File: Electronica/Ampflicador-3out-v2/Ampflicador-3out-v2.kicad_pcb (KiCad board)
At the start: 2 copper layers, 42 parts, among them P1 Piezo 1, P2 Piezo 2, P3 Piezo 2, Q1 MPF102, SW1 SW_DPST_x2, SW2 SW_DPST_x2, SW3 SW_SPDT, U1 LM386

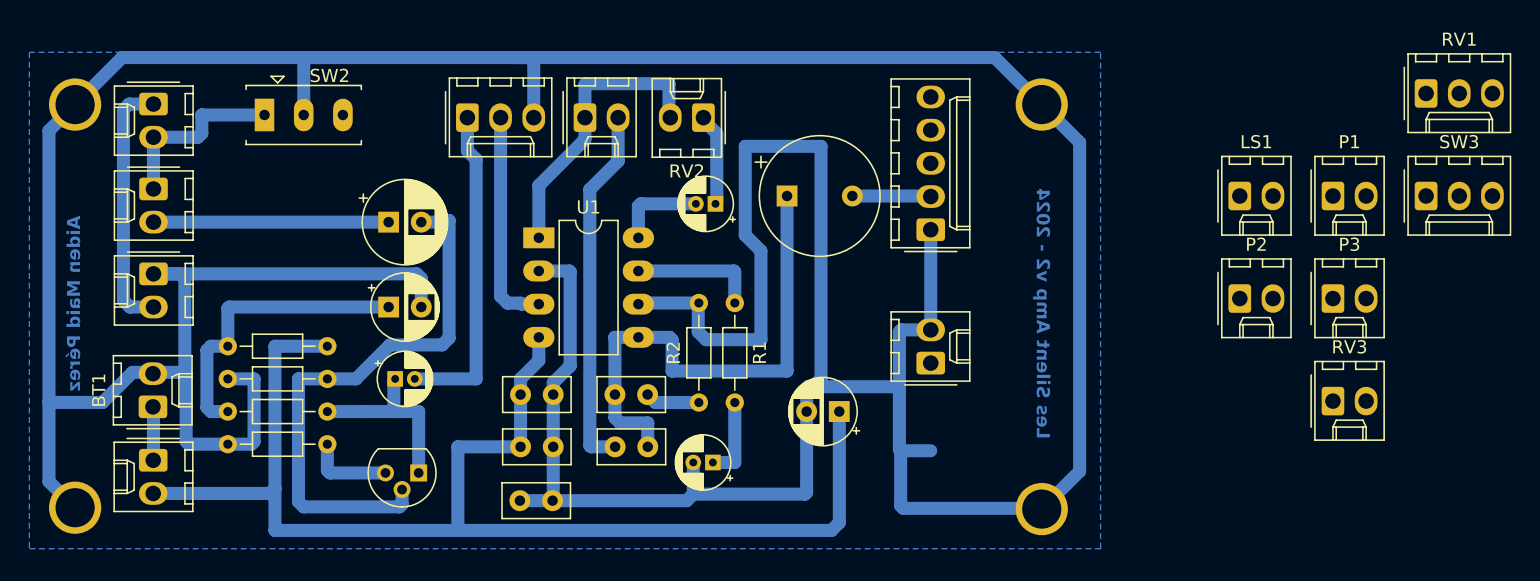
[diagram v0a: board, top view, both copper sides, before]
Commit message: Amp v2 sin termianr
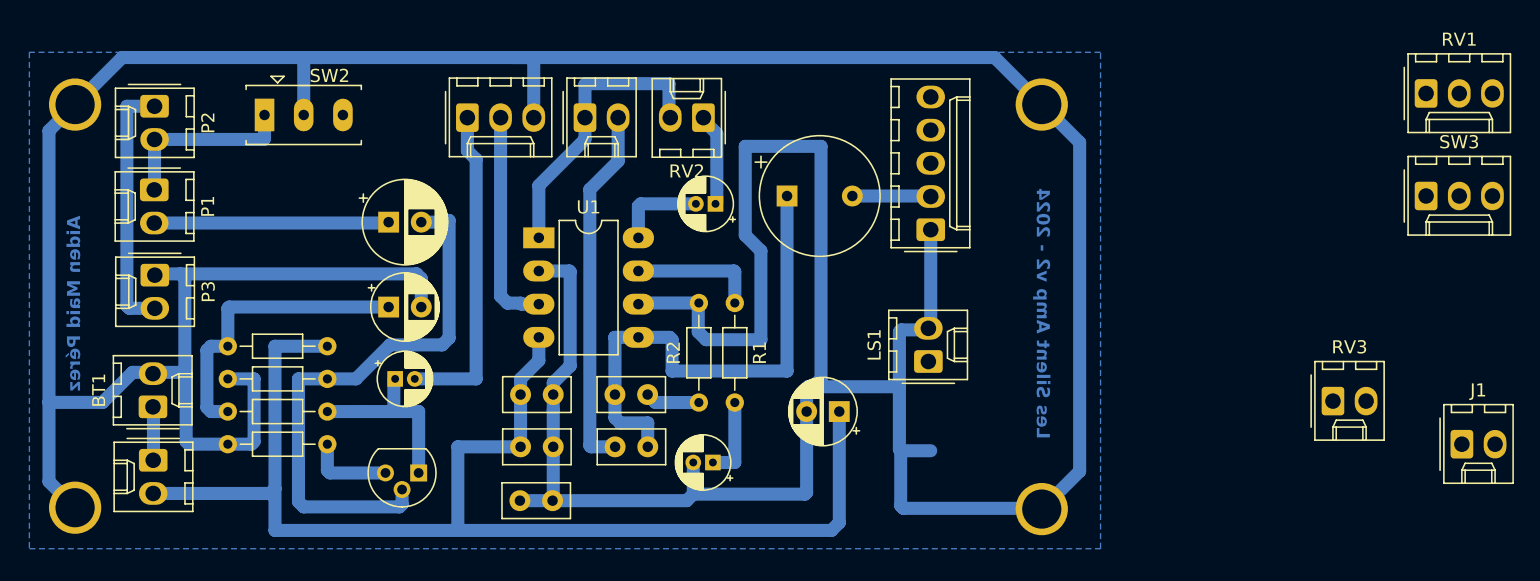
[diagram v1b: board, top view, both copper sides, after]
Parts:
- removed Input1, Input2, Input3, Output-Speaker1: Screw_Terminal_01x02, Connector_Molex:Molex_KK-254_AE-6410-02A_1x02_P2.54mm_Vertical
- added J1: Jack 6.5, Connector_Molex:Molex_KK-254_AE-6410-02A_1x02_P2.54mm_Vertical, F.Cu at (129.7, 54.0)
- moved P1 90.2 mm to (29.6, 34.5), turned to -90 degrees
- moved P3 90.2 mm to (29.6, 41.1), turned to -90 degrees
- moved P2 84.4 mm to (29.6, 28.1), turned to -90 degrees
- moved LS1 27.0 mm to (88.8, 47.7), turned to 90 degrees
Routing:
- net Net-(P2-Pad1): track 0.00 -> 19.6 mm
- net Net-(Input2-Pin_1): track 19.6 -> 0.00 mm
- net Net-(Input1-Pin_2): track 18.0 -> 0.00 mm
- net Net-(C10-Pad1): track 0.00 -> 18.0 mm
- net Net-(SW2A-A): track 0.00 -> 14.1 mm
- net Net-(Input1-Pin_1): track 14.0 -> 0.00 mm
- net GND: track 366.2 -> 364.2 mm

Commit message: Amp creo que para imprimir
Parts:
- removed Bass1: Screw_Terminal_01x02, Connector_Molex:Molex_KK-254_AE-6410-02A_1x02_P2.54mm_Vertical
- removed SW3: SW_SPDT, Connector_Molex:Molex_KK-254_AE-6410-03A_1x03_P2.54mm_Vertical
- removed Vol1: Screw_Terminal_01x03, Connector_Molex:Molex_KK-254_AE-6410-03A_1x03_P2.54mm_Vertical
- Gain: renamed from RV2; value Gain -> (none)
- J1: renamed from Output-Jack-3.5; value AudioJack2_Ground_Switch -> (none)
- J2: renamed from J1; value Jack 6.5 -> (none)
- LM386: renamed from U1; value LM386 -> (none)
- P2: value Piezo 2 -> (none)
- SP1: renamed from LS1; value Speaker -> (none)
- SW2: value SW_DPST_x2 -> (none)
- Volume: renamed from RV1; value Volume -> (none)
- moved Volume 73.5 mm to (53.5, 29.0)
- moved Bass 61.2 mm to (62.5, 29.0)
- moved J2 40.9 mm to (88.8, 54.5), turned to 90 degrees
- moved PW 2.61 mm to (29.5, 48.5), turned to -90 degrees
- moved Gain 2.50 mm to (69.1, 29.0), turned to 0 degrees
- moved C2 2.41 mm to (79.6, 51.4), turned to 0 degrees
- moved ? 1.70 mm to (95.8, 59.0)
- moved ? 1.70 mm to (95.8, 28.0)
- moved C6 0.22 mm to (72.3, 35.7)
- renumbered RV3 to Bass, BT1 to PW
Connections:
- J1 pad 2: (no net) -> Net-(C9-Pad2)
- J1 pad 3: (no net) -> Net-(J1-PadT)
- J1 pad 4: (no net) -> Net-(J1-PadT)
- J1 pad 5: (no net) -> Net-(C9-Pad2)
- J2 pad 1: (no net) -> GND
- J2 pad 2: (no net) -> Net-(J1-PadT)
- SP1 pad 1: Net-(SW3-C) -> Net-(J1-PadT)
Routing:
- net GND: track 364.2 -> 249.3 mm
- net Net-(J1-PadT): track 0.00 -> 30.3 mm
- net Net-(C8-Pad1): track 0.00 -> 28.0 mm
- net Net-(Bass1-Pin_2): track 28.0 -> 0.00 mm
- net Net-(RV2-Pad2): track 0.00 -> 25.2 mm
- net Net-(Vol1-Pin_1): track 24.9 -> 0.00 mm
- net Net-(C12-Pad2): track 0.00 -> 24.9 mm
- net Net-(Bass1-Pin_1): track 22.3 -> 0.00 mm
- net Net-(C9-Pad2): track 6.02 -> 16.7 mm
- net Net-(BT1-+): track 4.20 -> 12.0 mm
- net Net-(SW1A-B): track 99.5 -> 97.0 mm
- net Net-(C6-Pad1): track 7.12 -> 9.42 mm
- net Net-(SW2A-A): track 14.1 -> 16.0 mm
- net Net-(P2-Pad1): track 19.6 -> 21.4 mm
- net Net-(Q1-G): track 42.4 -> 43.4 mm
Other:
- board outline added: 79.8 x 38.4 mm

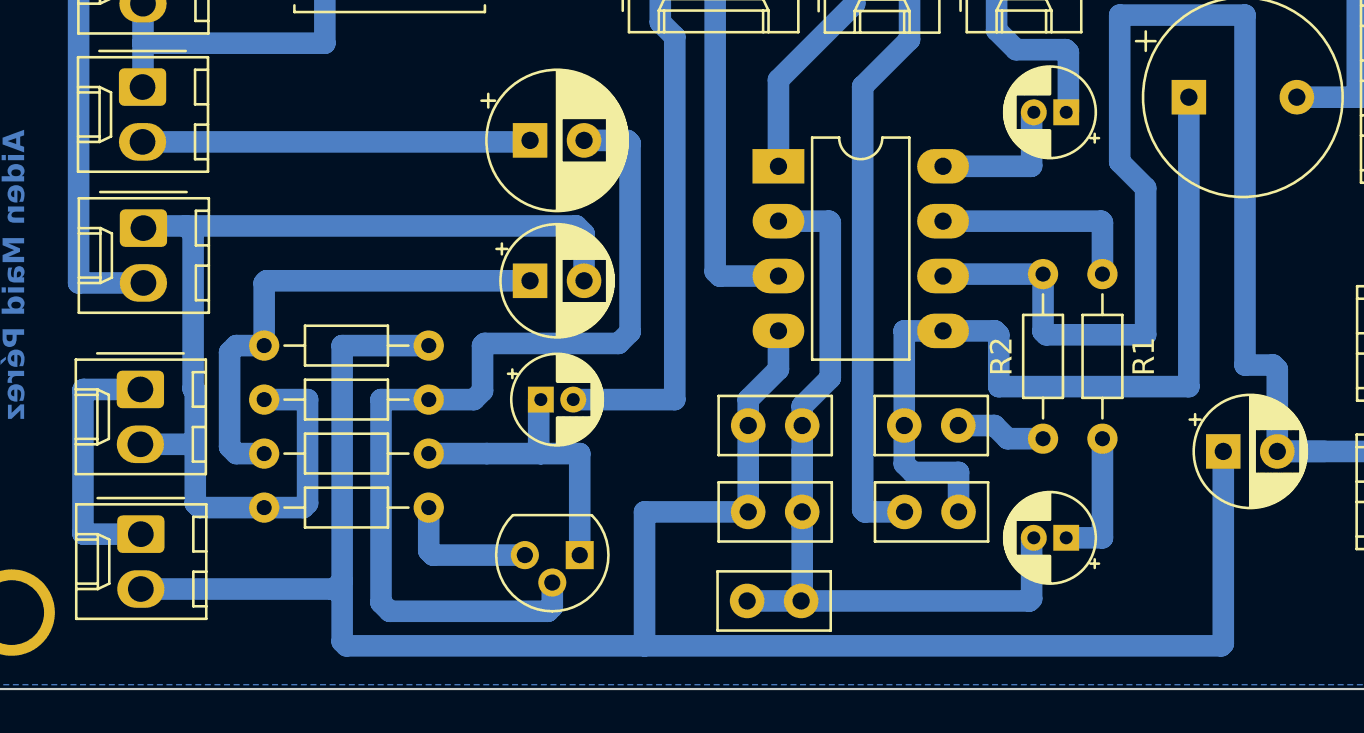
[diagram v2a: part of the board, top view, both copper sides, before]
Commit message: Amp V2 con Led
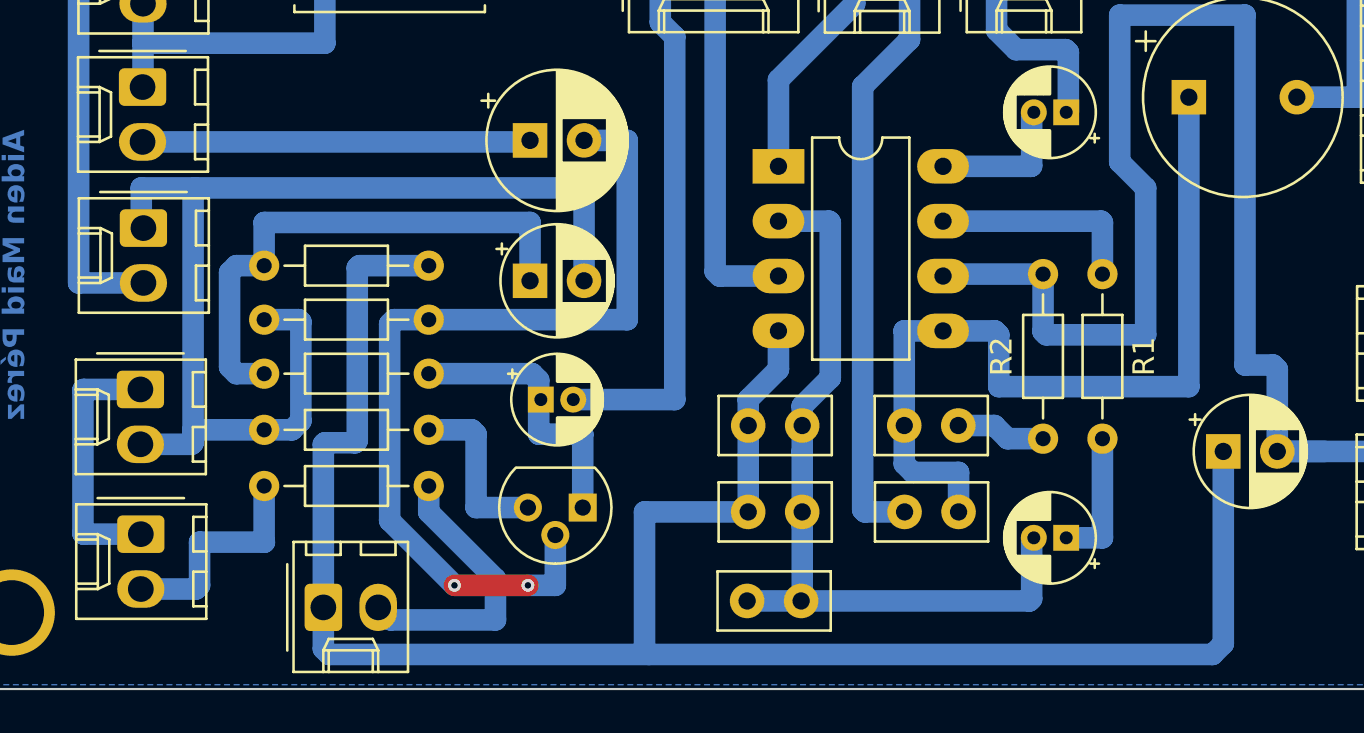
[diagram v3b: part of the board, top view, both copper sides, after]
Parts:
- added D1: LED, Connector_Molex:Molex_KK-254_AE-6410-02A_1x02_P2.54mm_Vertical, F.Cu at (37.9, 58.6)
- added R7: 430Ω, Resistor_THT:R_Axial_DIN0204_L3.6mm_D1.6mm_P7.62mm_Horizontal, F.Cu at (35.2, 53.0)
- J1: renamed from J2; value (none) -> Jack 6.5
- LS1: renamed from SP1; value (none) -> Speaker
- Output-Jack-3.5: renamed from J1; value (none) -> AudioJack2_Ground_Switch
- P2: value (none) -> Piezo 2
- RV1: renamed from Volume; value (none) -> Volume
- RV2: renamed from Gain; value (none) -> Gain
- SW2: value (none) -> SW_DPST_x2
- U1: renamed from LM386; value (none) -> LM386
- moved R3 3.70 mm to (42.8, 45.3)
- moved R5 3.70 mm to (35.2, 47.8)
- moved R6 3.70 mm to (35.2, 42.8)
- moved R4 3.60 mm to (42.8, 50.4)
- moved Q1 2.20 mm to (49.9, 54.0)
- renumbered PW to BT1, Bass to RV3
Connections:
- C1 pad 1: Net-(SW1A-B) -> Net-(D1-K)
- C2 pad 1: Net-(SW1A-B) -> Net-(D1-K)
- C3 pad 2: Net-(SW1A-B) -> Net-(D1-K)
- J1 pad 1: GND -> (no net)
- J1 pad 2: Net-(J1-PadT) -> (no net)
- Output-Jack-3.5 pad 2: Net-(C9-Pad2) -> (no net)
- Output-Jack-3.5 pad 3: Net-(J1-PadT) -> (no net)
- Output-Jack-3.5 pad 4: Net-(J1-PadT) -> (no net)
- Output-Jack-3.5 pad 5: Net-(C9-Pad2) -> (no net)
- R6 pad 2: Net-(SW1A-B) -> Net-(D1-K)
- U1 pad 4: Net-(SW1A-B) -> Net-(D1-K)
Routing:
- net Net-(D1-K): track 0.00 -> 93.8 mm
- net Net-(SW1A-B): track 97.0 -> 10.4 mm
- net Net-(D1-A): track 0.00 -> 13.2 mm
- net Net-(Q1-G): track 43.4 -> 41.3 mm, vias 0 -> 2
- net GND: track 249.3 -> 251.0 mm
- net Net-(C11-Pad1): track 23.1 -> 24.8 mm
- net Net-(Q1-S): track 6.53 -> 8.07 mm
- net Net-(Q1-D): track 14.2 -> 13.2 mm
